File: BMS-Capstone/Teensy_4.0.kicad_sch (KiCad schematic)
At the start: 1 part

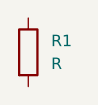
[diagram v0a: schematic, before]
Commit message: added hierarchial sheet for BMS[A
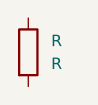
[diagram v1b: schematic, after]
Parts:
- renumbered R1 to R
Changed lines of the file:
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@@
 		(dnp no)
 		(fields_autoplaced yes)
-		(property "Reference" "R1"
+		(property "Reference" "R"
 			(at 157.48 83.8199 0)
 			(effects
@@
 		(pin "2"
 		)
-		(instances
-			(project ""
-				(path "/f2da9442-ca05-4687-a880-d5cd24c39f1d/26bdc180-da09-44b1-8397-e88b39d0135c"
-					(reference "R1")
-					(unit 1)
-				)
-			)
-		)
+		(instances)
 	)
 )

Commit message: Added bq chip
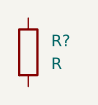
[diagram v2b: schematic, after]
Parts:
- renumbered R to R?
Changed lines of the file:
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@@
 		(dnp no)
 		(fields_autoplaced yes)
-		(property "Reference" "R"
+		(property "Reference" "R?"
 			(at 157.48 83.8199 0)
 			(effects
@@
 		(pin "2"
 		)
-		(instances)
+		(instances
+			(project "BMS"
+				(path "/f2da9442-ca05-4687-a880-d5cd24c39f1d/26bdc180-da09-44b1-8397-e88b39d0135c"
+					(reference "R?")
+					(unit 1)
+				)
+			)
+		)
 	)
 )
